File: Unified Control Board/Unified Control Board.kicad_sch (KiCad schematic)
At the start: 166 parts, among them CN1 B02B-PASK(LF)(SN), CN10 B3B-XH-2(LF)(SN), CN11 B3B-XH-2(LF)(SN), CN2 B02B-PASK(LF)(SN), CN3 B02B-PASK(LF)(SN), CN4 B04B-PASK(LF)(SN), CN5 B04B-PASK(LF)(SN), CN6 B02B-PASK(LF)(SN), CN7 B04B-PASK(LF)(SN), CN8 B04B-PASK(LF)(SN), CN9 B3B-XH-2(LF)(SN), SW1 TSA002A3512A02, SW2 TSA002A3512A02, SW3 TSA002A3512A02, U1 XT60PB-M.G.Y, U10 2.4GHz, U11 MP6541A, U12 MP6541A, U2 DRV8876PWPR, U3 DRV8876PWPR, U4 DRV8876PWPR, U5 DRV8876PWPR, U6 TCA9546A, U7 ZDSD01GLGEAG, U8 ESP32-S3-WROOM-1, U9 AP64350SP-13

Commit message: Baseline: uncommitted 24V design state from working tree (C28 pad fix, BOM merge, regenerated fab outputs)
Captures the edits made after 500dc69 so the 36V changes that follow
are reviewable on their own.

Co-Authored-By: Claude Opus 5.5 <noreply@anthropic.com>
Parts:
- C56, C63: value 22uF/16V -> 22uF
- U10: value 2.4GHz -> ESP32-S3-WROOM-1
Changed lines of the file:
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@@
 			)
 		)
-		(property "Value" "2.4GHz"
+		(property "Value" "ESP32-S3-WROOM-1"
 			(at 482.6 -64.77 0)
 			(show_name no)
@@
 			)
 		)
-		(property "Value" "22uF/16V"
+		(property "Value" "22uF"
 			(at 674.37 157.48 0)
 			(show_name no)
@@
 			)
 		)
-		(property "Value" "22uF/16V"
+		(property "Value" "22uF"
 			(at 914.4 73.66 90)
 			(show_name no)

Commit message: 36V redesign: parts, schematic and footprint swaps (routing still to do)
Every IC on the input rail was rated too close to 36 V, so:
- U2-U5 DRV8876 (40 V abs) -> DRV8251ADDAR (48/50 V). Internal charge
  pump: C2/C3/C4/C6/C12/C13/C14/C15 removed. IPROPI gain 1575 uA/A, so
  R1/R11/R12/R21 1.5k -> 1k (ITRIP 2.10 A). No nFAULT: FAULT net undriven.
- U11/U12 MP6541A (45 V abs) -> MP6540HA (50/60 V), same pinout and caps;
  new QFN-26 5x5 footprint from the MPS land pattern.
- U9 AP64350 (42 V abs) -> TPS54360BDDAR (60/65 V), same SO-8EP pinout.
  EN now floats (8.4 V abs max), D5 RB050L-60 catch diode added,
  compensation re-designed: R31 7.5k, C29 12nF, C30 82pF.
- D3 SMCJ24A -> SMCJ36A; D1/D2 SS14 -> RB050L-60 (60 V, low Vf).
- Bulk: C27 330uF/50V, C39/C60 100uF/50V, C28 220uF/50V, plus new C74/C75
  330uF/50V (VCC bulk ~1.28 mF). C51/C68 -> 100 V.
- New inrush soft-start (DRV8251A VM ramp limit 2 V/us): Q1 ME50P06-G
  P-FET between XT60 (new net VIN_RAW) and VCC, R59/R60/C72/C73/D6.
- DRU: MP6541A 0.1 mm exception replaced by a 0.4 mm 36V pad rule.

PCB: new footprints placed, old fan-out copper removed, zones refilled.
DRC schematic parity is clean; 99 unconnected items remain to route, plus
one pre-existing TL IN2 track 0.2 mm from C39's VCC pad. Fab outputs in
jlcpcb/ are stale until re-routed.

Co-Authored-By: Claude Opus 5.5 <noreply@anthropic.com>
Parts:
- removed C12: 22nF, MaslowMerged:C0805, symbol CL21B223KBANNNC_3
- removed C13: 22nF, MaslowMerged:C0805, symbol CL21B223KBANNNC
- removed C14: 100nF, ProPrj_Dri-easyedapro:C0603, symbol CC0805KRX7R9BB104_6
- removed C15: 100nF, ProPrj_Dri-easyedapro:C0603, symbol CC0805KRX7R9BB104_7
- removed C2: 22nF, MaslowMerged:C0805, symbol CL21B223KBANNNC_1
- removed C3: 100nF, ProPrj_Dri-easyedapro:C0603, symbol CC0805KRX7R9BB104_4
- removed C4: 22nF, MaslowMerged:C0805, symbol CL21B223KBANNNC_2
- removed C6: 100nF, ProPrj_Dri-easyedapro:C0603, symbol CC0805KRX7R9BB104_5
- added C72: 10uF/25V, MaslowMerged:C0805, symbol ProPrj_Dri-easyedapro:CL05B104KB54PNC
- added C73: 220nF/100V, MaslowMerged:C0805, symbol ProPrj_Dri-easyedapro:CL05B104KB54PNC
- added C74, C75: 330uF/50V, MaslowMerged:CAP-SMD_BD10.0-L10.3-W10.3-LS10.9-FD, symbol GVM1V681M1010
- added D5: RB050L-60TE25, MaslowMerged:SMA_L4.2-W2.6-LS5.3-RD, symbol ProPrj_Dri-easyedapro:SS36
- added D6: BZT52C15, Diode_SMD:D_SOD-123, symbol Device:D_Zener
- added Q1: ME50P06-G, Package_TO_SOT_SMD:TO-252-2, symbol MaslowMerged:Q_PMOS_GDS
- added R59: 47kΩ, ProPrj_Dri-easyedapro:R0402, symbol ProPrj_Dri-easyedapro:0402WGF1002TCE
- added R60: 100kΩ, ProPrj_Dri-easyedapro:R0402, symbol ProPrj_Dri-easyedapro:0402WGF1002TCE
- C27: value 680uF -> 330uF/50V; MPN GVM1V681M1010 -> EEEFT1H331AP; Manufacturer HONOR(荣誉) -> PANASONIC; Supplier Part C2980172 -> C178596
- C28: value 680uF -> 220uF/50V; MPN GVM1V681M1010 -> UCD1H221MNL1GS; Manufacturer HONOR(荣誉) -> Nichicon; Supplier Part C2980172 -> C116211
- C29: value 3.3nF -> 12nF; MPN CC0402KRX7R9BB332 -> CC0402KRX7R9BB123; Supplier Part C107028 -> C576739
- C30: value 68pF -> 82pF; MPN CC0402JRNPO9BN680 -> CC0402JRNPO9BN820; Supplier Part C107009 -> C107011
- C39, C60: value 220uF -> 100uF/50V; LCSC Part Name 220uF ±20% 35V -> 100uF ±20% 50V (alt: Chengx KM107M050F12RR0VH2FP0 C2749); MPN ERS1VM221F12OT -> 50YXF100MEFC8X11.5; Manufacturer AISHI(艾华集团) -> Rubycon; Supplier Part C106697 -> C88728
- C50, C67: value 1uF/16V -> 1uF/50V
- C51, C68: LCSC Part Name 100nF ±10% 50V X7R 0603 MLCC -> 100nF ±10% 100V X7R 0603 MLCC; MPN CC0603KRX7R9BB104 -> CL10B104KC8NNNC; Manufacturer YAGEO(国巨) -> SAMSUNG(三星); Supplier Part C14663 -> C15725
- D1, D2: value SS14 -> RB050L-60TE25; MPN SS14 -> RB050L-60TE25; Manufacturer MDD(辰达半导体) -> ROHM; Supplier Part C2480 -> C209642
- D3: value SMCJ24A -> SMCJ36A; LCSC Part Name SMCJ24A -> SMCJ36A; MPN SMCJ24A -> SMCJ36A; Manufacturer RUILON(瑞隆源) -> Littelfuse; Supplier Part C10771 -> C151282
- R1, R11, R12, R21: value 1.5kΩ -> 1kΩ; MPN 0402WGF1501TCE -> 0402WGF1001TCE; Supplier Part C25867 -> C11702
- R31: value 10kΩ -> 7.5kΩ; LCSC Part Name 3.3kΩ ±1% 1/16W 0402 Chip Resistor -> 7.5kΩ ±1% 1/16W 0402 Chip Resistor; MPN 0402WGF1002TCE -> 0402WGF7501TCE; Supplier Part C25744 -> C25918
- U11, U12: value MP6541A -> MP6540HA; footprint ProPrj_Dri-easyedapro:TQFN-26 (6X6MM) -> MaslowMerged:QFN-26_5x5mm_MP6540H; symbol ProPrj_Dri-easyedapro:MP6541A -> MaslowMerged:MP6540HA; MPN MP6541AGQKT-Z -> MP6540HGU-A-Z; Supplier Part C22444490 -> consigned (not stocked at LCSC)
- U2: value DRV8876PWPR -> DRV8251ADDAR; footprint MaslowMerged:HTSSOP-16_L5.0-W4.4-P0.65-LS6.4-BL-EP -> MaslowMerged:SOIC-8-1EP_DDA0008B_ThermalVias_0.3mm; symbol DRV8876PWPR_1 -> MaslowMerged:DRV8251ADDAR; MPN DRV8876PWPR -> DRV8251ADDAR; Supplier Part C575551 -> C5218844
- U3: value DRV8876PWPR -> DRV8251ADDAR; footprint MaslowMerged:HTSSOP-16_L5.0-W4.4-P0.65-LS6.4-BL-EP -> MaslowMerged:SOIC-8-1EP_DDA0008B_ThermalVias_0.3mm; symbol DRV8876PWPR_2 -> MaslowMerged:DRV8251ADDAR; MPN DRV8876PWPR -> DRV8251ADDAR; Supplier Part C575551 -> C5218844
- U4: value DRV8876PWPR -> DRV8251ADDAR; footprint MaslowMerged:HTSSOP-16_L5.0-W4.4-P0.65-LS6.4-BL-EP -> MaslowMerged:SOIC-8-1EP_DDA0008B_ThermalVias_0.3mm; symbol DRV8876PWPR_3 -> MaslowMerged:DRV8251ADDAR; MPN DRV8876PWPR -> DRV8251ADDAR; Supplier Part C575551 -> C5218844
- U5: value DRV8876PWPR -> DRV8251ADDAR; footprint MaslowMerged:HTSSOP-16_L5.0-W4.4-P0.65-LS6.4-BL-EP -> MaslowMerged:SOIC-8-1EP_DDA0008B_ThermalVias_0.3mm; symbol DRV8876PWPR -> MaslowMerged:DRV8251ADDAR; MPN DRV8876PWPR -> DRV8251ADDAR; Supplier Part C575551 -> C5218844
- U9: value AP64350SP-13 -> TPS54360BDDAR; symbol MaslowMerged:AP64350 -> MaslowMerged:TPS54360B; MPN AP64350SP-13 -> TPS54360BDDAR; Manufacturer DIODES -> Texas Instruments; Supplier Part C2071691 -> C524806
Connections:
- net 3V3: now also U2.4 (VREF), U3.4 (VREF), U4.4 (VREF), U5.4 (VREF); no longer U2.16 (PMODE), U2.3 (nSLEEP), U2.5 (VREF), U3.16 (PMODE), U3.3 (nSLEEP), U3.5 (VREF), U4.16 (PMODE), U4.3 (nSLEEP), U4.5 (VREF), U5.16 (PMODE), U5.3 (nSLEEP), U5.5 (VREF)
- net BL IN1: now also U4.3 (IN1); no longer U4.1 (EN/IN1)
- net BL OUT1: now also U4.6 (OUT1); no longer U4.8 (OUT1)
- net BL OUT2: now also U4.8 (OUT2); no longer U4.10 (OUT2)
- net BR IN1: now also U5.3 (IN1); no longer U5.1 (EN/IN1)
- net BR OUT1: now also U5.6 (OUT1); no longer U5.8 (OUT1)
- net BR OUT2: now also U5.8 (OUT2); no longer U5.10 (OUT2)
- net FAULT: no longer U2.4 (nFAULT), U3.4 (nFAULT), U4.4 (nFAULT), U5.4 (nFAULT)
- net GND: now also C74.2, C75.2, D5.2 (A), R60.2; no longer U2.15 (GND), U2.17 (EP), U3.15 (GND), U3.17 (EP), U4.15 (GND), U4.17 (EP), U5.15 (GND), U5.17 (EP)
- net SW_NODE: now also D5.1 (K)
- net TL IN1: now also U3.3 (IN1); no longer U3.1 (EN/IN1)
- net TL OUT1: now also U3.6 (OUT1); no longer U3.8 (OUT1)
- net TL OUT2: now also U3.8 (OUT2); no longer U3.10 (OUT2)
- net TR IN1: now also U2.3 (IN1); no longer U2.1 (EN/IN1)
- net TR OUT1: now also U2.6 (OUT1); no longer U2.8 (OUT1)
- net TR OUT2: now also U2.8 (OUT2); no longer U2.10 (OUT2)
- net VCC: now also U2.5 (VM), U3.5 (VM), U4.5 (VM), U5.5 (VM), C73.2, C74.1, C75.1, Q1.2 (D); no longer U1.1, U2.11 (VM), U3.11 (VM), U4.11 (VM), U5.11 (VM)
- net VSUP: no longer U9.3 (EN)
- net at R1.2, R20.2: now also U5.1 (IPROPI); no longer U5.6 (IPROPI)
- net at R19.2, R21.2: now also U4.1 (IPROPI); no longer U4.6 (IPROPI)
- net at R11.2, R9.2: now also U2.1 (IPROPI); no longer U2.6 (IPROPI)
- net at R10.2, R12.2: now also U3.1 (IPROPI); no longer U3.6 (IPROPI)
- new net SS_GATE: C72.2, C73.1, D6.2 (A), Q1.1 (G), R59.2, R60.1
- new net VIN_RAW: C72.1, D6.1 (K), Q1.3 (S), R59.1, U1.1
- no-connect marks 31 -> 32
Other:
- note added: "36V INRUSH SOFT-START (DRV8251A VM ramp must stay < 2V/us) Q1 source on XT60 (VIN_RAW), drain to VCC. C72 holds Vgs ~0 at plug-in; R60 pulls the gate down, C73 (Miller) sets the VCC ramp: ~(VIN-3.5V)/R60/C73 = ~1.5 V/ms at 36V -> ~25 ms, ~2A into ~1.2 mF. Steady Vgs = VIN*R59/(R59+R60) = 11.5V @36V; D6 clamps Vgs at 15V."
- note added: "36V: U2-U5 are DRV8251A (no nFAULT/nSLEEP, internal charge pump). IPROPI gain 1575uA/A: R1/R11/R12/R21 = 1k -> ITRIP 2.10A, 1.575 V/A. The FAULT net (U8 IO40, R28) no longer has a driver."
- note added: "U9 = TPS54360B (60V). EN is intentionally floating: internal 1.2uA pull-up. EN abs max is 8.4V - never tie EN to VSUP. D5 = required catch diode. Comp re-designed for 484kHz, 3.28V, ~60uF Cout, fc ~20kHz: R31 7.5k, C29 12nF, C30 82pF."

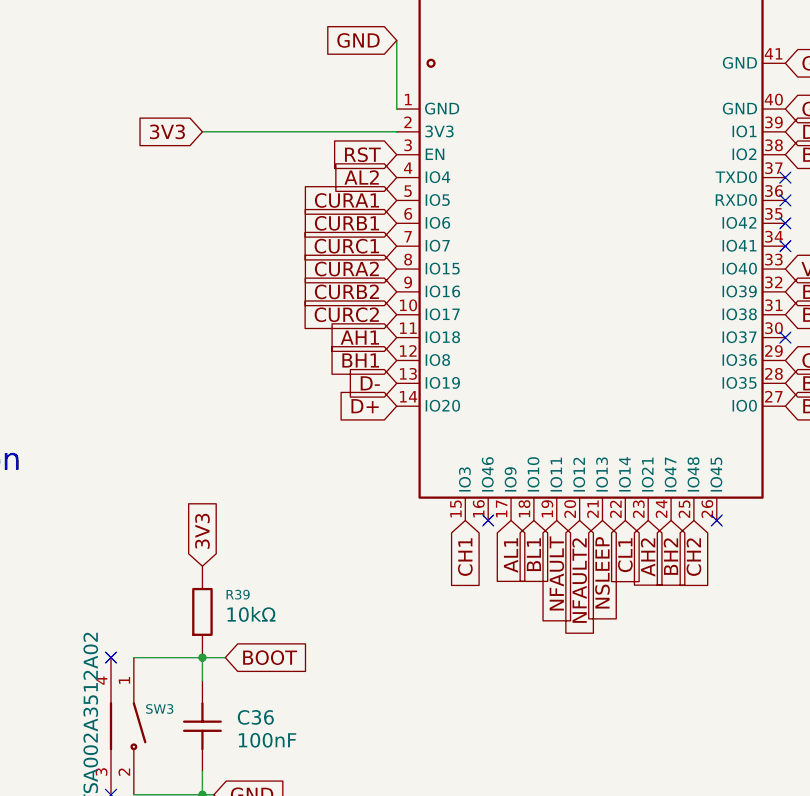
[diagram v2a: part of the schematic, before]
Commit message: Move motor 2 current sense onto ADC1 pins
CURA2/CURB2/CURC2 were on U10 IO15/16/17 (ADC2, unusable while Wi-Fi is
active). Swapped with three PWM outputs that work on any GPIO:
  CURA2 IO15 -> IO4 (ADC1_CH3)    AL2 IO4 -> IO15
  CURB2 IO16 -> IO8 (ADC1_CH7)    BH1 IO8 -> IO16
  CURC2 IO17 -> IO9 (ADC1_CH8)    AL1 IO9 -> IO17

PCB: U10 pad nets updated and the six old stubs cut at the pads; the
connections are left to route (DRC parity clean, 6 new unconnected).

Co-Authored-By: Claude Opus 5.5 <noreply@anthropic.com>
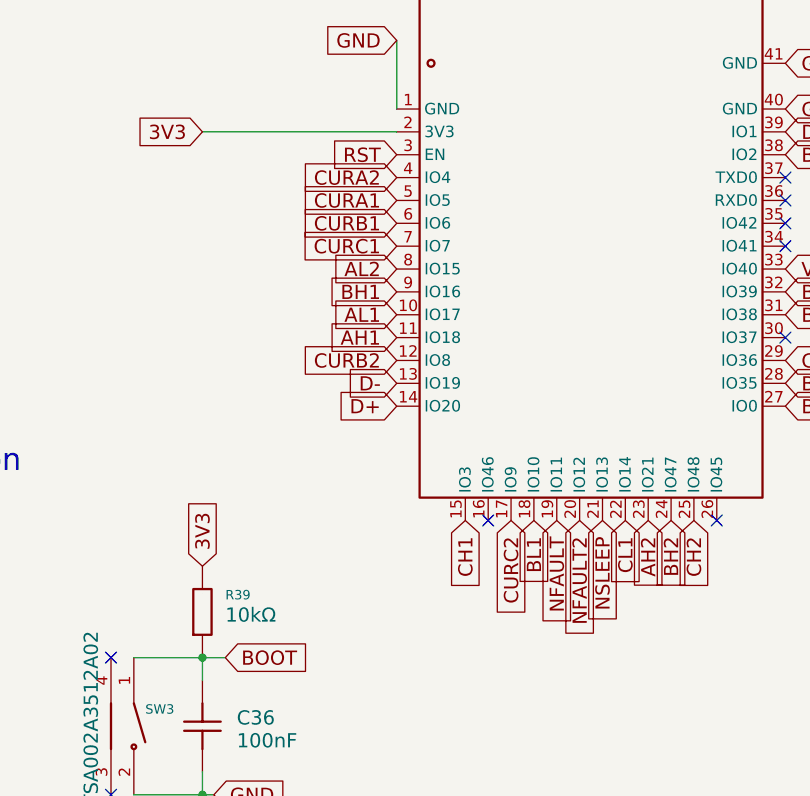
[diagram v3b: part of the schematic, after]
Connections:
- net AL1: now also U10.10 (IO17); no longer U10.17 (IO9)
- net AL2: now also U10.8 (IO15); no longer U10.4 (IO4)
- net BH1: now also U10.9 (IO16); no longer U10.12 (IO8)
- net CURA2: now also U10.4 (IO4); no longer U10.8 (IO15)
- net CURB2: now also U10.12 (IO8); no longer U10.9 (IO16)
- net CURC2: now also U10.17 (IO9); no longer U10.10 (IO17)
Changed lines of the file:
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@@
 		)
 	)
-	(global_label "BH1"
+	(global_label "CURB2"
 		(shape input)
 		(at 467.36 -8.89 180)
@@
 		)
 	)
-	(global_label "AL2"
+	(global_label "CURA2"
 		(shape input)
 		(at 467.36 -29.21 180)
@@
 		)
 	)
-	(global_label "AL1"
+	(global_label "CURC2"
 		(shape input)
 		(at 480.06 8.89 270)
@@
 		)
 	)
-	(global_label "CURA2"
+	(global_label "AL2"
 		(shape input)
 		(at 467.36 -19.05 180)
@@
 		)
 	)
-	(global_label "CURC2"
+	(global_label "AL1"
 		(shape input)
 		(at 467.36 -13.97 180)
@@
 		)
 	)
-	(global_label "CURB2"
+	(global_label "BH1"
 		(shape input)
 		(at 467.36 -16.51 180)

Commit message: Add buffered ADS7038 phase-current ADC on U10 SPI
1 MSPS 8-ch 12-bit SPI ADC (ADS7038QRTERQ1) samples all six MP6540HA
current-sense outputs so firmware can read every phase inside the
low-side window.

- Reference = AVDD = 3V3: 0-3.3V span covers the 1.65V +/- 0.179 V/A
  signals and is ratiometric with the 3.3k/3.3k SOx bias. (ADS795x would
  need a separate 3.0V reference; 2xVREF range is not allowed at 3.3V.)
- Each SOx output now feeds a TLV9064 unity-gain buffer (U13 motor 1,
  U14 motor 2). The old 330R/1nF ESP32 filter loaded the SOx node and
  settled with tau ~2us (1nF through 1.65k bias + 330R); buffered:
  - ADC path: 47R / 1nF C0G, settles and recovers the 12pF kickback
    within the 300ns acquisition time.
  - ESP32 path: R40-42/R54-56 330R -> 2.0k so the ESP32 ADC keeps the
    same ~2us response it had before, now from a low-impedance source.
- AIN0-2 = motor 1 A/B/C, AIN3-5 = motor 2 A/B/C, AIN6/7 spare.
- SPI on U10: IO37 CS (10k pull-up), IO41 SCLK, IO42 SDI, IO46 SDO.
  IO46 is a boot strap: SDO is hi-Z while CS is high, so the internal
  pull-down still sets it at reset. U10 is the N8R2 (quad PSRAM), so
  IO35-37 are usable.

PCB: 21 parts placed beside the sense networks, U10 and the six filter
resistors re-netted with old stubs cut. DRC parity clean, only baseline
errors; 56 new connections to route.

Co-Authored-By: Claude Opus 5.5 <noreply@anthropic.com>
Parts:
- added C76, C77: 100nF, ProPrj_Dri-easyedapro:C0603, symbol ProPrj_Dri-easyedapro:CL05B104KB54PNC
- added C78, C79, C80, C81, C82, C83: 1nF C0G, ProPrj_Dri-easyedapro:C0402, symbol ProPrj_Dri-easyedapro:CL05B104KB54PNC
- added C84, C85, C86: 1uF, ProPrj_Dri-easyedapro:C0402, symbol ProPrj_Dri-easyedapro:CL05B104KB54PNC
- added R61, R62, R63, R64, R65, R66: 47Ω, ProPrj_Dri-easyedapro:R0402, symbol ProPrj_Dri-easyedapro:0402WGF1002TCE
- added R67: 10kΩ, ProPrj_Dri-easyedapro:R0402, symbol ProPrj_Dri-easyedapro:0402WGF1002TCE
- added U13, U14: TLV9064IDR, Package_SO:SOIC-14_3.9x8.7mm_P1.27mm, symbol MaslowMerged:TLV9064
- added U15: ADS7038QRTERQ1, Package_DFN_QFN:WQFN-16-1EP_3x3mm_P0.5mm_EP1.68x1.68mm, symbol MaslowMerged:ADS7038
- R40, R41, R42, R54, R55, R56: value 330Ω -> 2kΩ; LCSC Part Name 330Ω ±1% 62.5mW 厚膜电阻 -> 2kΩ ±1% 1/16W 0402 Chip Resistor; MPN 0402WGF3300TCE -> 0402WGF2001TCE; Supplier Part C25104 -> C4109
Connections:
- net 3V3: now also C76.1, C77.1, C84.1, C85.1, R67.1, U13.4 (V+), U14.4 (V+), U15.10 (DVDD), U15.7 (AVDD)
- net GND: now also C76.2, C77.2, C78.2, C79.2, C80.2, C81.2, C82.2, C83.2, C84.2, C85.2, C86.2, U13.11 (V-), U13.12 (IN4+), U14.11 (V-), U14.12 (IN4+), U15.17 (EP), U15.9 (GND)
- net SOA: now also U13.3 (IN1+); no longer R42.2
- net SOA2: now also U14.3 (IN1+); no longer R56.2
- net SOB: now also U13.5 (IN2+); no longer R41.2
- net SOB2: now also U14.5 (IN2+); no longer R55.2
- net SOC: now also U13.10 (IN3+); no longer R40.2
- net SOC2: now also U14.10 (IN3+); no longer R54.2
- net ADC_SDO: now reaches U10.16 (IO46)
- net ADC_SDO: now also U15.12 (SDO)
- net ADC_CS: now reaches U10.30 (IO37)
- net ADC_CS: now also R67.2, U15.11 (~{CS})
- net ADC_SCLK: now reaches U10.34 (IO41)
- net ADC_SCLK: now also U15.13 (SCLK)
- net ADC_SDI: now reaches U10.35 (IO42)
- net ADC_SDI: now also U15.14 (SDI)
- new net ADC_A1: C78.1, R61.2, U15.15 (AIN0)
- new net ADC_A2: C81.1, R64.2, U15.2 (AIN3)
- new net ADC_B1: C79.1, R62.2, U15.16 (AIN1)
- new net ADC_B2: C82.1, R65.2, U15.3 (AIN4)
- new net ADC_C1: C80.1, R63.2, U15.1 (AIN2)
- new net ADC_C2: C83.1, R66.2, U15.4 (AIN5)
- new net ADC_DECAP: C86.1, U15.8 (DECAP)
- new net SOA2_BUF: R56.2, R64.1, U14.1 (OUT1), U14.2 (IN1-)
- new net SOA_BUF: R42.2, R61.1, U13.1 (OUT1), U13.2 (IN1-)
- new net SOB2_BUF: R55.2, R65.1, U14.6 (IN2-), U14.7 (OUT2)
- new net SOB_BUF: R41.2, R62.1, U13.6 (IN2-), U13.7 (OUT2)
- new net SOC2_BUF: R54.2, R66.1, U14.8 (OUT3), U14.9 (IN3-)
- new net SOC_BUF: R40.2, R63.1, U13.8 (OUT3), U13.9 (IN3-)
- new net U13_SPARE: U13.13 (IN4-), U13.14 (OUT4)
- new net U14_SPARE: U14.13 (IN4-), U14.14 (OUT4)
- no-connect marks 32 -> 30
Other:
- note added: "PHASE-CURRENT ADC (36V branch) SOx -> TLV9064 follower -> (a) 2.0k/1nF -> ESP32 ADC (same ~2us response as before) -> (b) 47R/1nF C0G -> ADS7038 (settles <0.3us, 12pF kickback recovered in tACQ) ADS7038 ref = AVDD = 3V3: 0-3.3V span, ratiometric with the 3.3k/3.3k SOx bias (1.65V = 0A, 0.179 V/A). SPI on U10: IO37 CS (10k pull-up) IO41 SCLK IO42 SDI IO46 SDO. IO46 is a strapping pin: SDO is hi-Z 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"

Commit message: Drive the ADS7038 straight from the MP6540HA sense outputs
Drop the ESP32 copy of the six phase-current signals and, with it, the
TLV9064 buffers and the ADC-side RC filters. Each SOx node (3.3k/3.3k
bias, ~1.65k) now connects directly to its ADS7038 input:
  SOA/SOB/SOC -> AIN0/AIN1/AIN2, SOA2/SOB2/SOC2 -> AIN3/AIN4/AIN5.
With no capacitor at the ADC pin the node settles in ~35 ns, and the
sampling-cap kickback recovers well inside the on-the-fly acquisition
time. The buffers were only needed to stop the ESP32 path's 2.0k/1nF
filter slowing the node (45% of each step with a 3.7 us time constant).

Removed (26 parts): U13, U14 (TLV9064), R61-R66 47R, C78-C83 1nF,
R40-R42 and R54-R56 2.0k, C35/C37/C38/C57/C58/C59 1nF.
U10 IO4-IO9 are now free (no-connect); the phase currents must be read
from the ADS7038, so the spindle firmware's analogRead current sensing
and over-current check need porting before this board can run.

PCB: footprints and their copper removed, U15/U10 pads re-netted, zones
refilled. DRC parity clean; unrouted 161 -> 125. One new
starved-thermal warning on R37's GND pad, in the area still to route.

Co-Authored-By: Claude Opus 5.5 <noreply@anthropic.com>
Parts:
- removed C35, C37, C38, C57, C58, C59: 1nF, ProPrj_Dri-easyedapro:C0402, symbol ProPrj_Dri-easyedapro:0402CG220J500NT
- removed C78, C79, C80, C81, C82, C83: 1nF C0G, ProPrj_Dri-easyedapro:C0402, symbol ProPrj_Dri-easyedapro:CL05B104KB54PNC
- removed R40, R41, R42, R54, R55, R56: 2kΩ, ProPrj_Dri-easyedapro:R0402, symbol ProPrj_Dri-easyedapro:0402WGF3300TCE
- removed R61, R62, R63, R64, R65, R66: 47Ω, ProPrj_Dri-easyedapro:R0402, symbol ProPrj_Dri-easyedapro:0402WGF1002TCE
- removed U13, U14: TLV9064IDR, Package_SO:SOIC-14_3.9x8.7mm_P1.27mm, symbol MaslowMerged:TLV9064
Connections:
- net ADC_A1 is gone; now on net SOA: U15.15 (AIN0)
- net ADC_A2 is gone; now on net SOA2: U15.2 (AIN3)
- net ADC_B1 is gone; now on net SOB: U15.16 (AIN1)
- net ADC_B2 is gone; now on net SOB2: U15.3 (AIN4)
- net ADC_C1 is gone; now on net SOC: U15.1 (AIN2)
- net ADC_C2 is gone; now on net SOC2: U15.4 (AIN5)
- net CURA1: no longer names the net of U10.5 (IO5)
- net CURA2: no longer names the net of U10.4 (IO4)
- net CURB1: no longer names the net of U10.6 (IO6)
- net CURB2: no longer names the net of U10.12 (IO8)
- net CURC1: no longer names the net of U10.7 (IO7)
- net CURC2: no longer names the net of U10.17 (IO9)
- no-connect marks 30 -> 36
